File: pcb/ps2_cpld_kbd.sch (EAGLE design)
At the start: 34 parts, among them J1 AVR ISP, J2 JTAG, J3 Emulated Mechanical Keyboard, J4 Power, J5 PS/2, U1 ATMEGA328, U2 EPM7128, Y1 16MHz

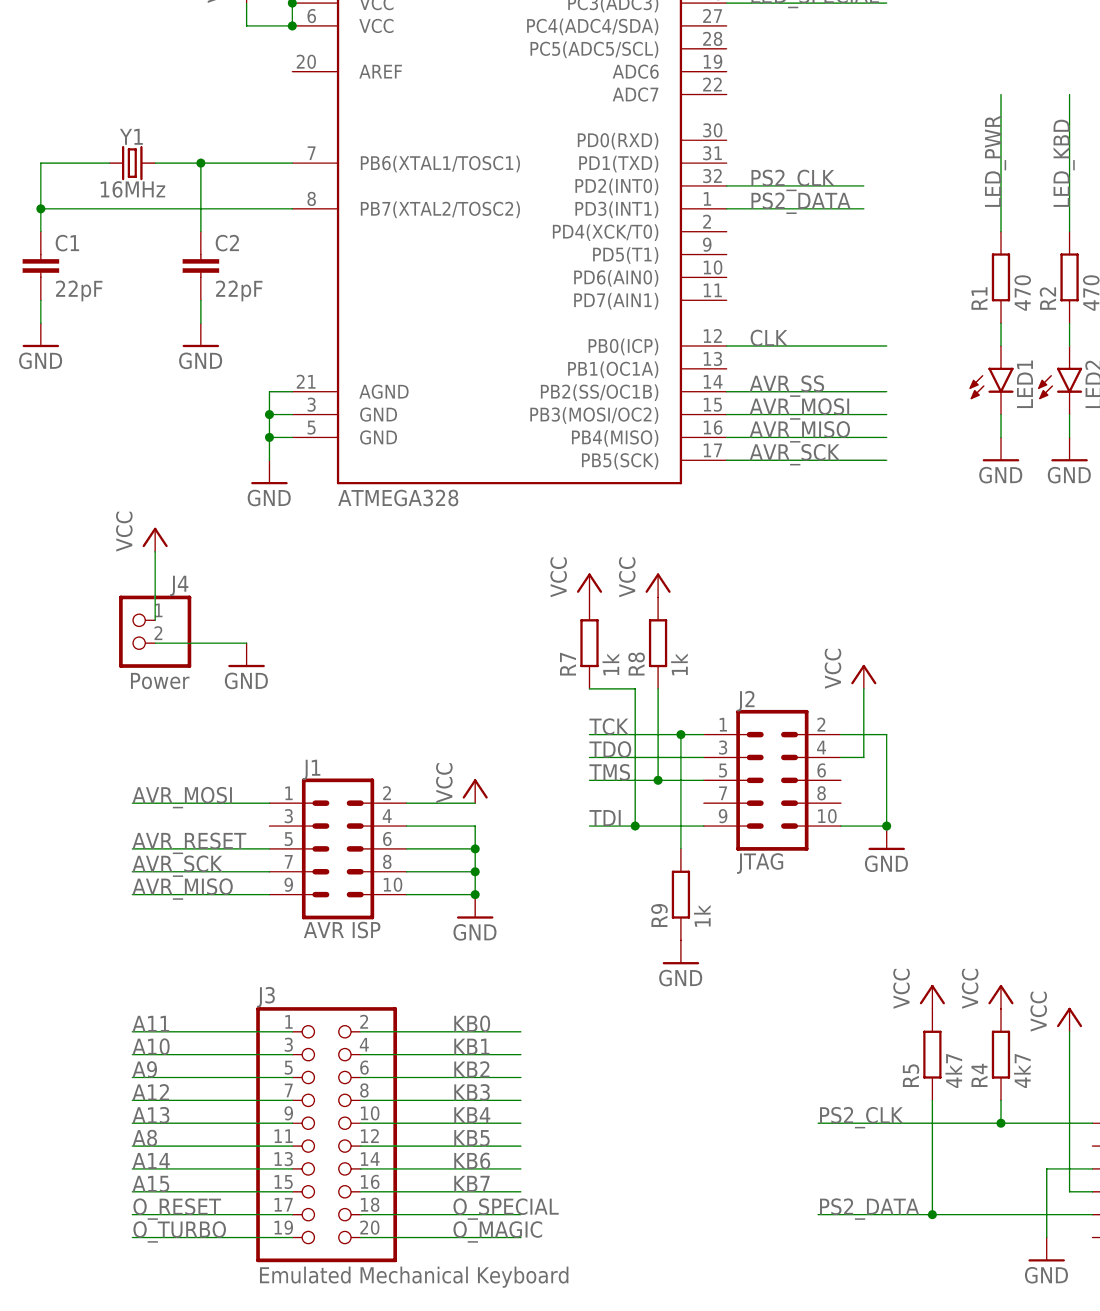
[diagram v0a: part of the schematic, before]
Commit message: fixed ps/2 signal names, fixed github page url
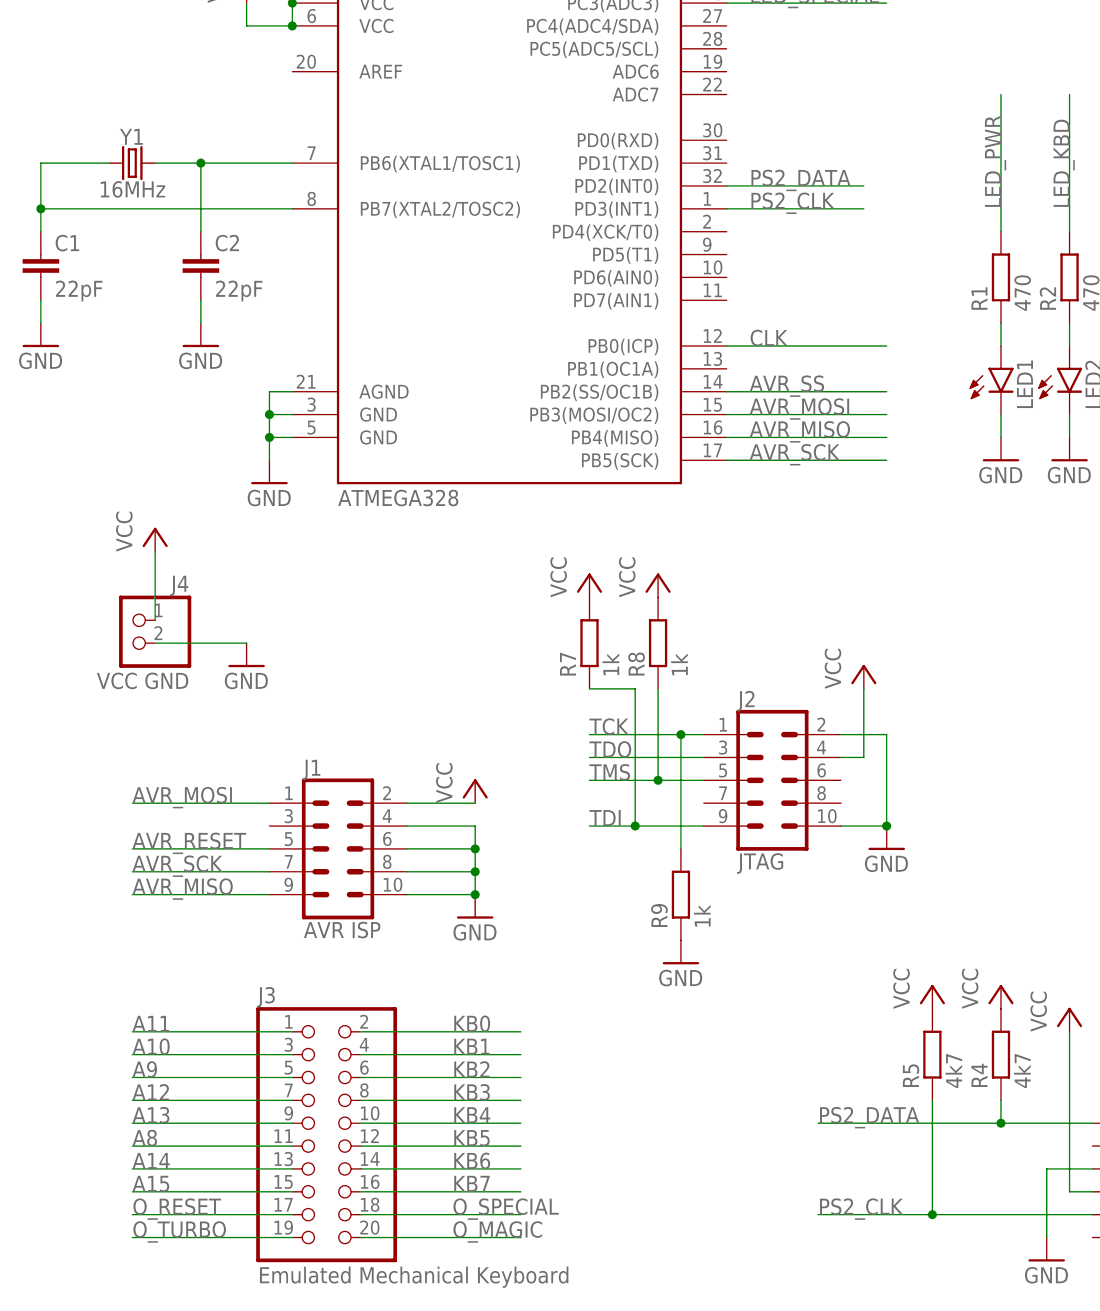
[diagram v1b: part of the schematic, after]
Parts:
- J4: value Power -> VCC GND
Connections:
- net PS2_CLK: now also J5.5, R5.1, U1.PD3(INT1); no longer J5.1, R4.1, U1.PD2(INT0)
- net PS2_DATA: now also J5.1, R4.1, U1.PD2(INT0); no longer J5.5, R5.1, U1.PD3(INT1)
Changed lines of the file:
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@@
 <part name="U2" library="altera" library_urn="urn:adsk.eagle:library:97" deviceset="EPM7128-?100" device="T" package3d_urn="urn:adsk.eagle:package:8081283/1" value="EPM7128"/>
 <part name="J3" library="pinhead" library_urn="urn:adsk.eagle:library:325" deviceset="PINHD-2X10" device="" package3d_urn="urn:adsk.eagle:package:22405/2" value="Emulated Mechanical Keyboard"/>
-<part name="J4" library="pinhead" library_urn="urn:adsk.eagle:library:325" deviceset="PINHD-1X2" device="" package3d_urn="urn:adsk.eagle:package:22435/2" value="Power"/>
+<part name="J4" library="pinhead" library_urn="urn:adsk.eagle:library:325" deviceset="PINHD-1X2" device="" package3d_urn="urn:adsk.eagle:package:22435/2" value="VCC GND"/>
 <part name="Y1" library="SparkFun-Clocks" library_urn="urn:adsk.eagle:library:511" deviceset="CRYSTAL-16MHZ" device="PTH-HC49US" package3d_urn="urn:adsk.eagle:package:37515/1" value="16MHz"/>
 <part name="J5" library="con-yamaichi" library_urn="urn:adsk.eagle:library:202" deviceset="MD06SS" device="" package3d_urn="urn:adsk.eagle:package:11778/1" value="PS/2"/>
@@
 </segment>
 </net>
-<net name="PS2_CLK" class="0">
+<net name="PS2_DATA" class="0">
 <segment>
 <pinref part="U1" gate="U$1" pin="PD2(INT0)"/>
@@
 </segment>
 </net>
-<net name="PS2_DATA" class="0">
+<net name="PS2_CLK" class="0">
 <segment>
 <pinref part="U1" gate="U$1" pin="PD3(INT1)"/>

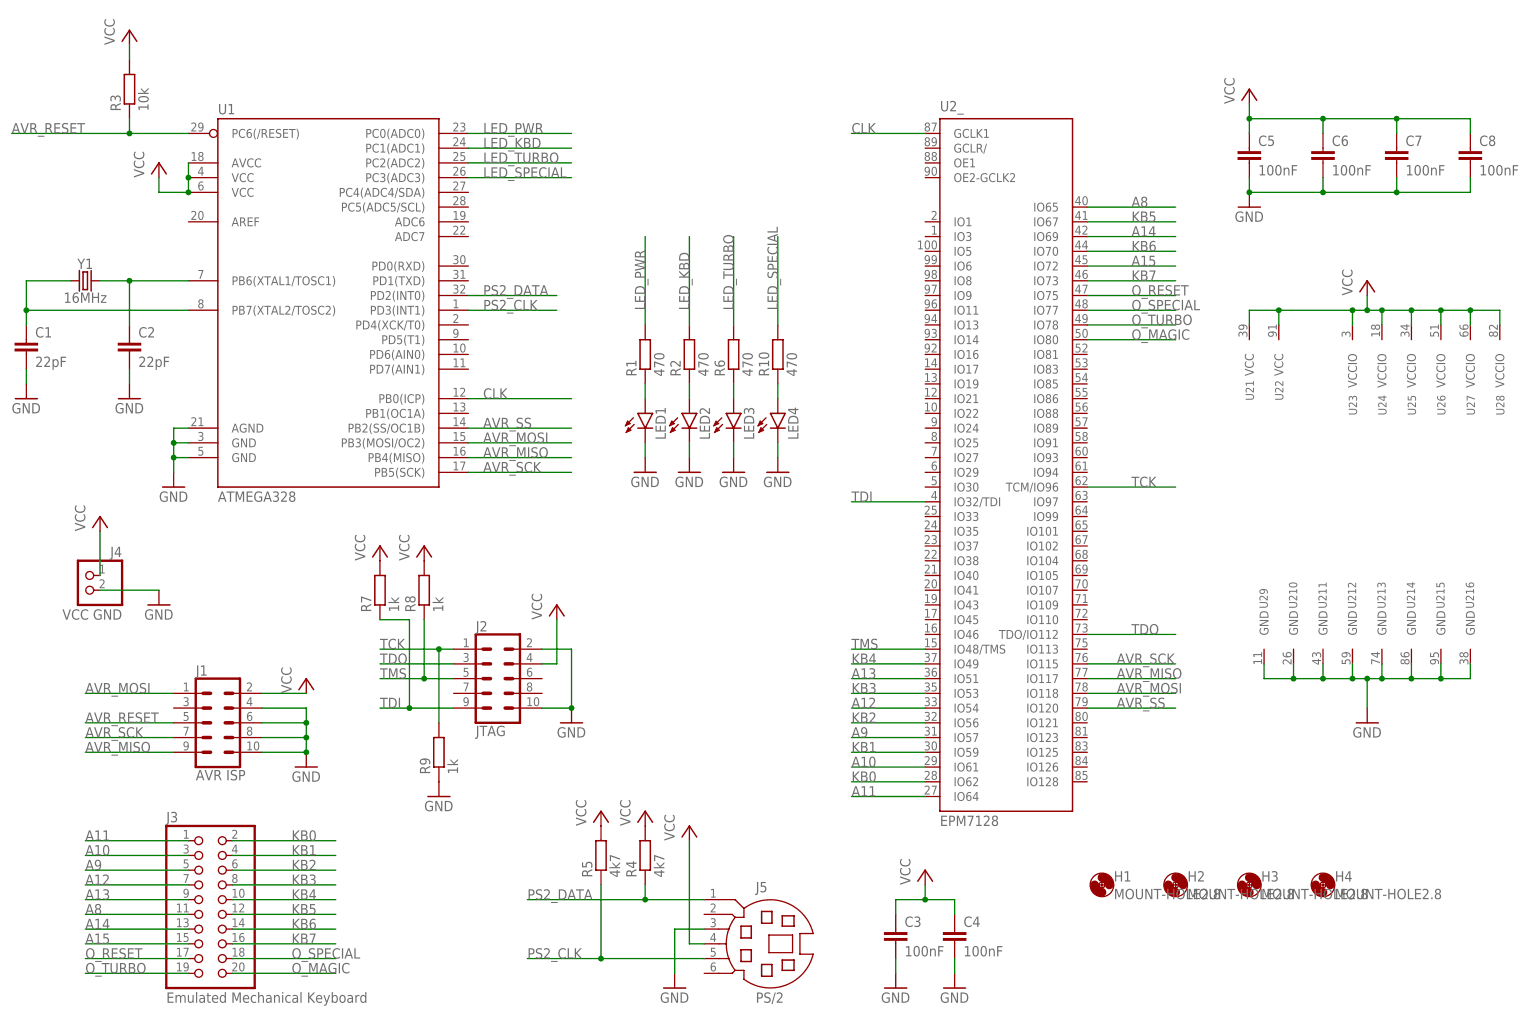
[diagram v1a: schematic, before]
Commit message: updated schamatics and board v1.1
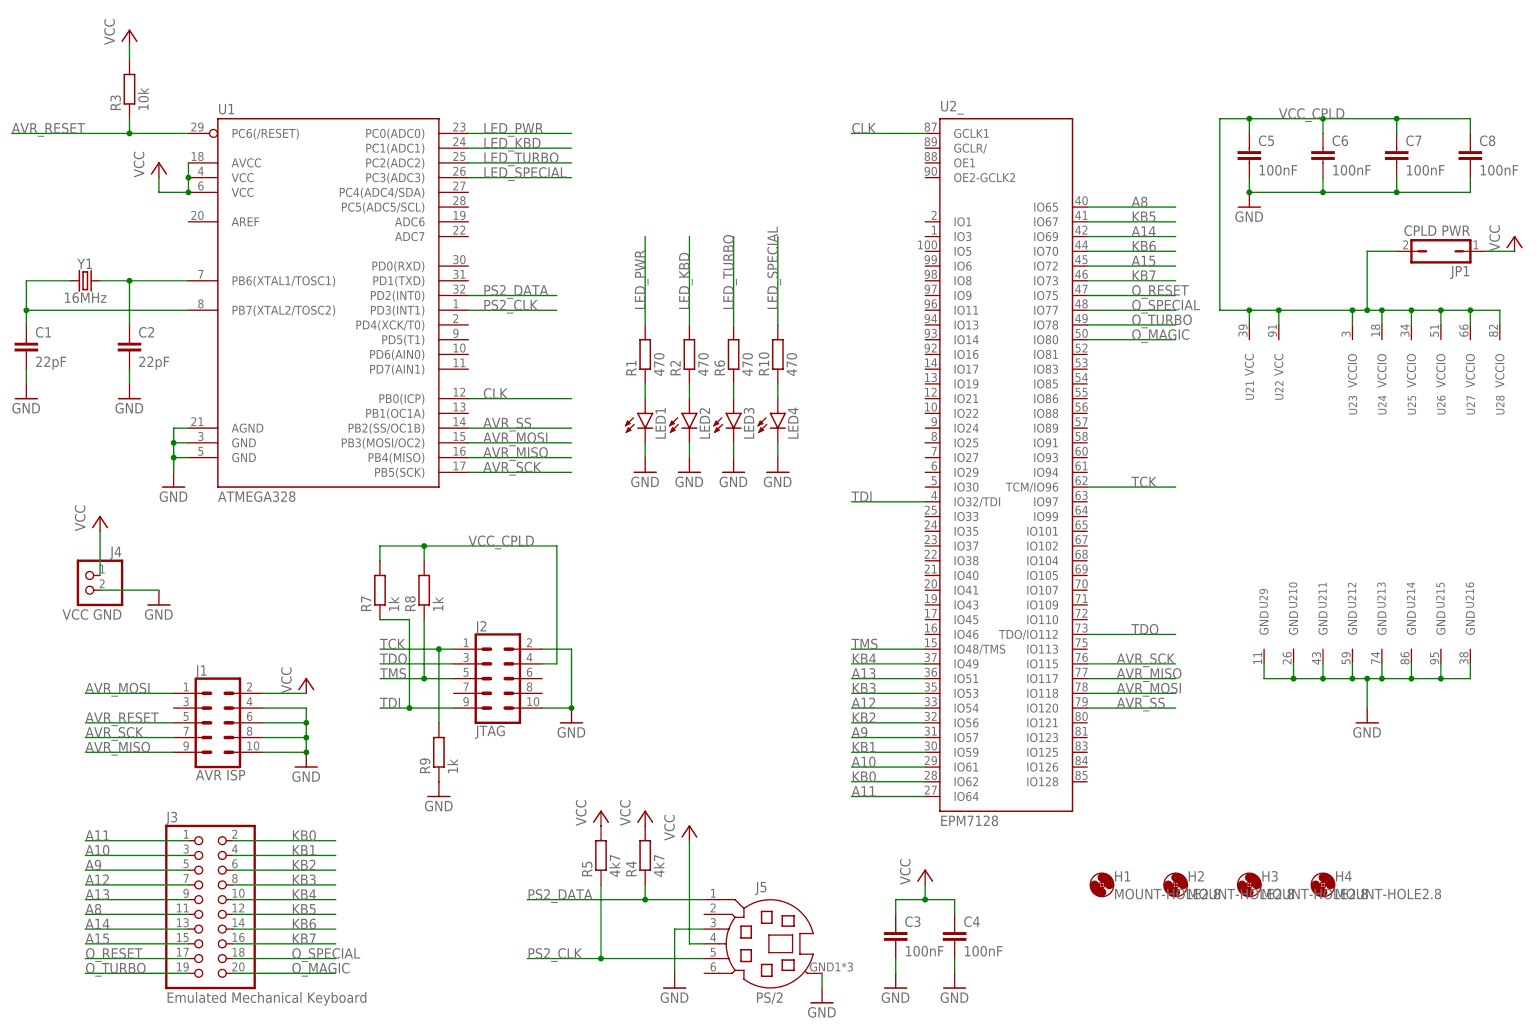
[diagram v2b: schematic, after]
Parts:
- added JP1: CPLD PWR, jumper:JP1Q
- J5: device con-yamaichi:MD06SS -> con-yamaichi-mod:MD06SS
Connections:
- new net VCC_CPLD: C5.1, C6.1, C7.1, C8.1, J2.4, JP1.2, R7.2, R8.2, U21.VCC, U22.VCC, U23.VCCIO, U24.VCCIO, U25.VCCIO, U26.VCCIO, U27.VCCIO, U28.VCCIO
- net GND: now also J5.GND
- net VCC: now also JP1.1; no longer C5.1, C6.1, C7.1, C8.1, J2.4, R7.2, R8.2, U21.VCC, U22.VCC, U23.VCCIO, U24.VCCIO, U25.VCCIO, U26.VCCIO, U27.VCCIO, U28.VCCIO

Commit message: new board v1.2 with fixes
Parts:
- added R11, R12, R13, R14, R15, R16, R17, R18: 10k, rcl:R-EU_R0805
- J4: device pinhead:PINHD-1X2 -> pinhead-mod:PINHD-1X2
- JP1: device jumper:JP1Q -> jumper-mod:JP1Q
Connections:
- net A10: now also R12.2
- net A11: now also R11.2
- net A12: now also R14.2
- net A13: now also R15.2
- net A14: now also R17.2
- net A15: now also R18.2
- net A8: now also R16.2
- net A9: now also R13.2
- net VCC: now also R11.1, R12.1, R13.1, R14.1, R15.1, R16.1, R17.1, R18.1
